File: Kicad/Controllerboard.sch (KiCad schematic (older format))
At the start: 0 parts

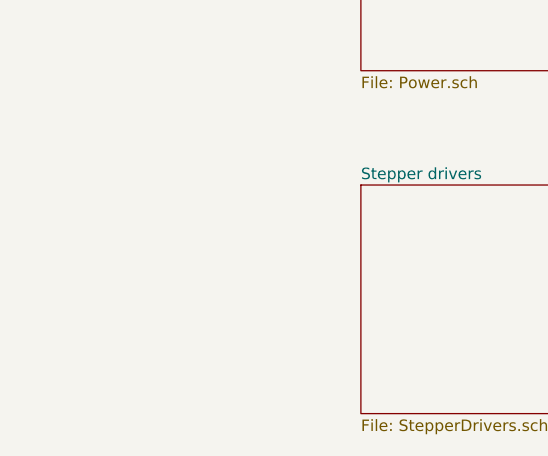
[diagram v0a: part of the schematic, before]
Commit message: Added spindle sheet
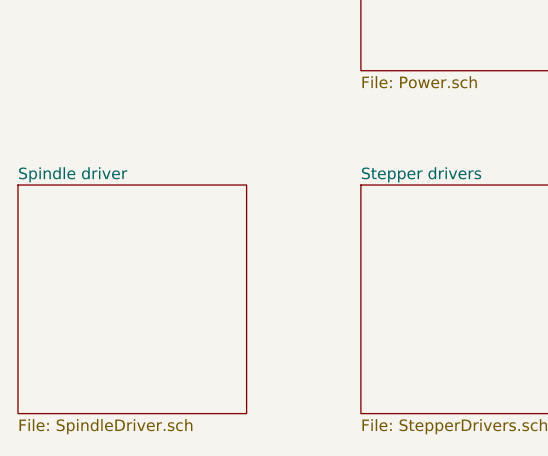
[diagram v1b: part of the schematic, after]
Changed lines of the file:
@@
 $Descr A4 11693 8268
 encoding utf-8
-Sheet 1 4
+Sheet 1 5
 Title ""
 Date ""
@@
 F1 "StepperDrivers.sch" 50
 $EndSheet
+$Sheet
+S 3000 5500 1000 1000
+U 5E280739
+F0 "Spindle driver" 50
+F1 "SpindleDriver.sch" 50
+$EndSheet
 $EndSCHEMATC
